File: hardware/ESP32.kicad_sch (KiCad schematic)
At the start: 17 parts, among them J1 USB_C_Receptacle_USB2.0_16P, SW1 SW_Omron_B3FS, SW2 SW_Omron_B3FS, U2 ESP32-C3-WROOM-02, U8 USBLC6-2SC6

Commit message: Found all diodes & transistors footprint & JLCPCB
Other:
- company: (none) -> ECAM Brussels Engineering School
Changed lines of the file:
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@@
 	(generator_version "9.0")
 	(paper "A4")
+	(title_block
+		(rev "0.1")
+		(company "ECAM Brussels Engineering School")
+	)
 	(junction
 		(at 129.54 49.53)

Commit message: Module Lora
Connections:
- net SCL: no longer names the net of R7.2, U2.17 (IO1)
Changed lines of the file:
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@@
+	(wire
+		(pts
+			(xy 184.15 76.2) (xy 198.12 76.2)
+		)
+		(stroke
+			(width 0)
+			(type default)
+		)
+	)
 	(wire
 		(pts
@@
 		)
 		(property "Intersheetrefs" "${INTERSHEET_REFS}"
-			(at 176.0848 68.58 0)
+			(at 175.4197 76.2 0)
 			(effects
 				(font
@@
 		)
 	)
-	(global_label "SCL"
+	(global_label "SPI_CLK"
 		(shape output)
-		(at 177.8 53.34 180)
+		(at 186.69 68.58 180)
 		(fields_autoplaced yes)
 		(effects
@@
 		)
 		(property "Intersheetrefs" "${INTERSHEET_REFS}"
-			(at 171.3072 53.34 0)
+			(at 176.0848 68.58 0)
 			(effects
 				(font

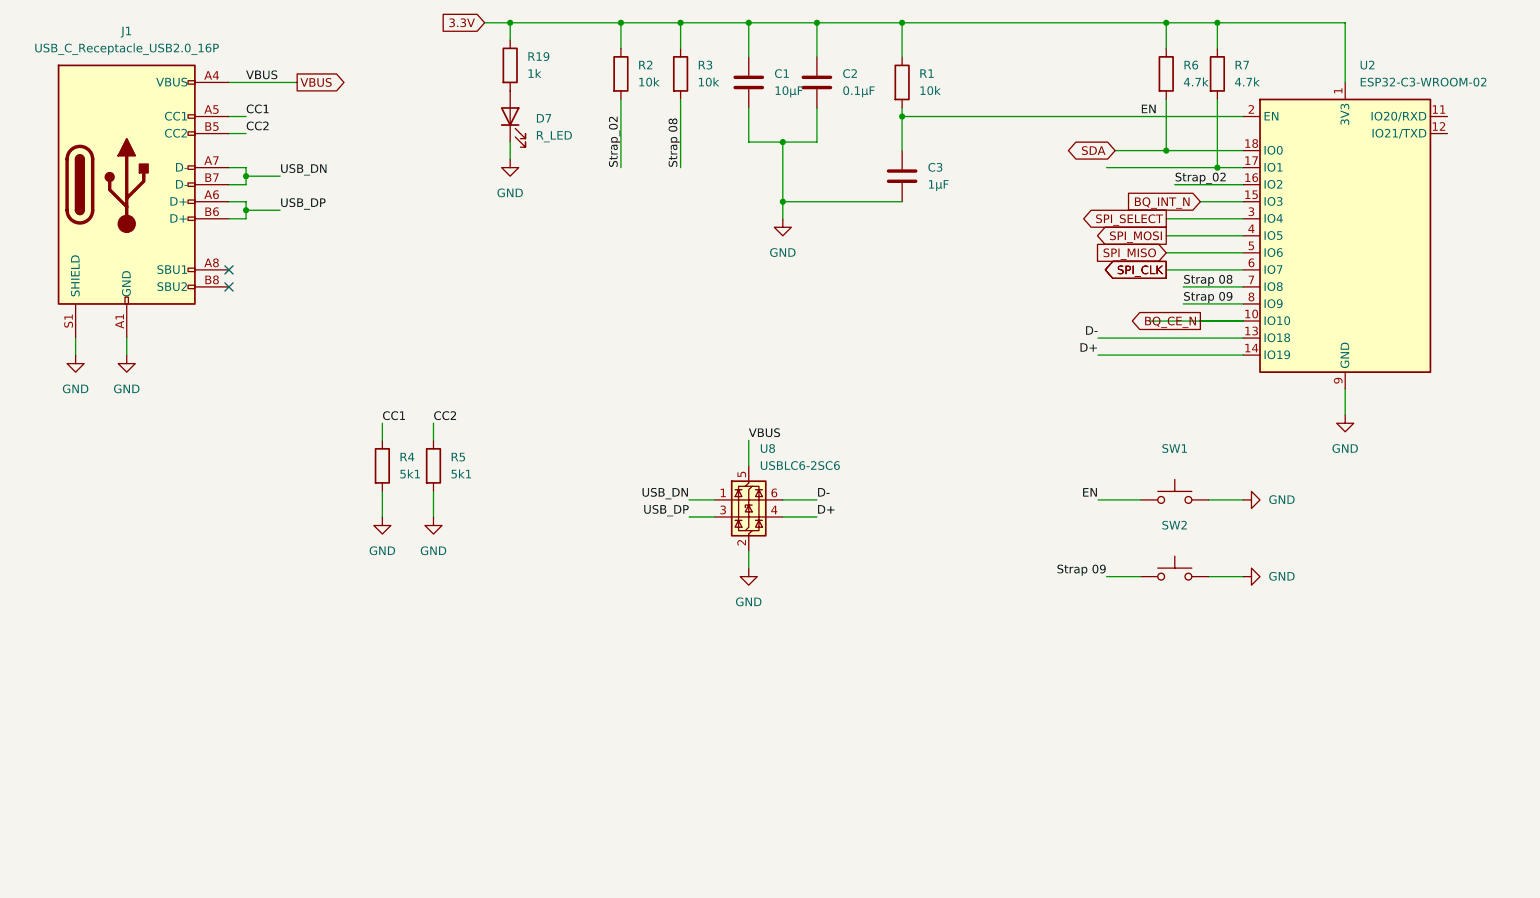
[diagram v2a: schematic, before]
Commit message: Update ESP32 pins
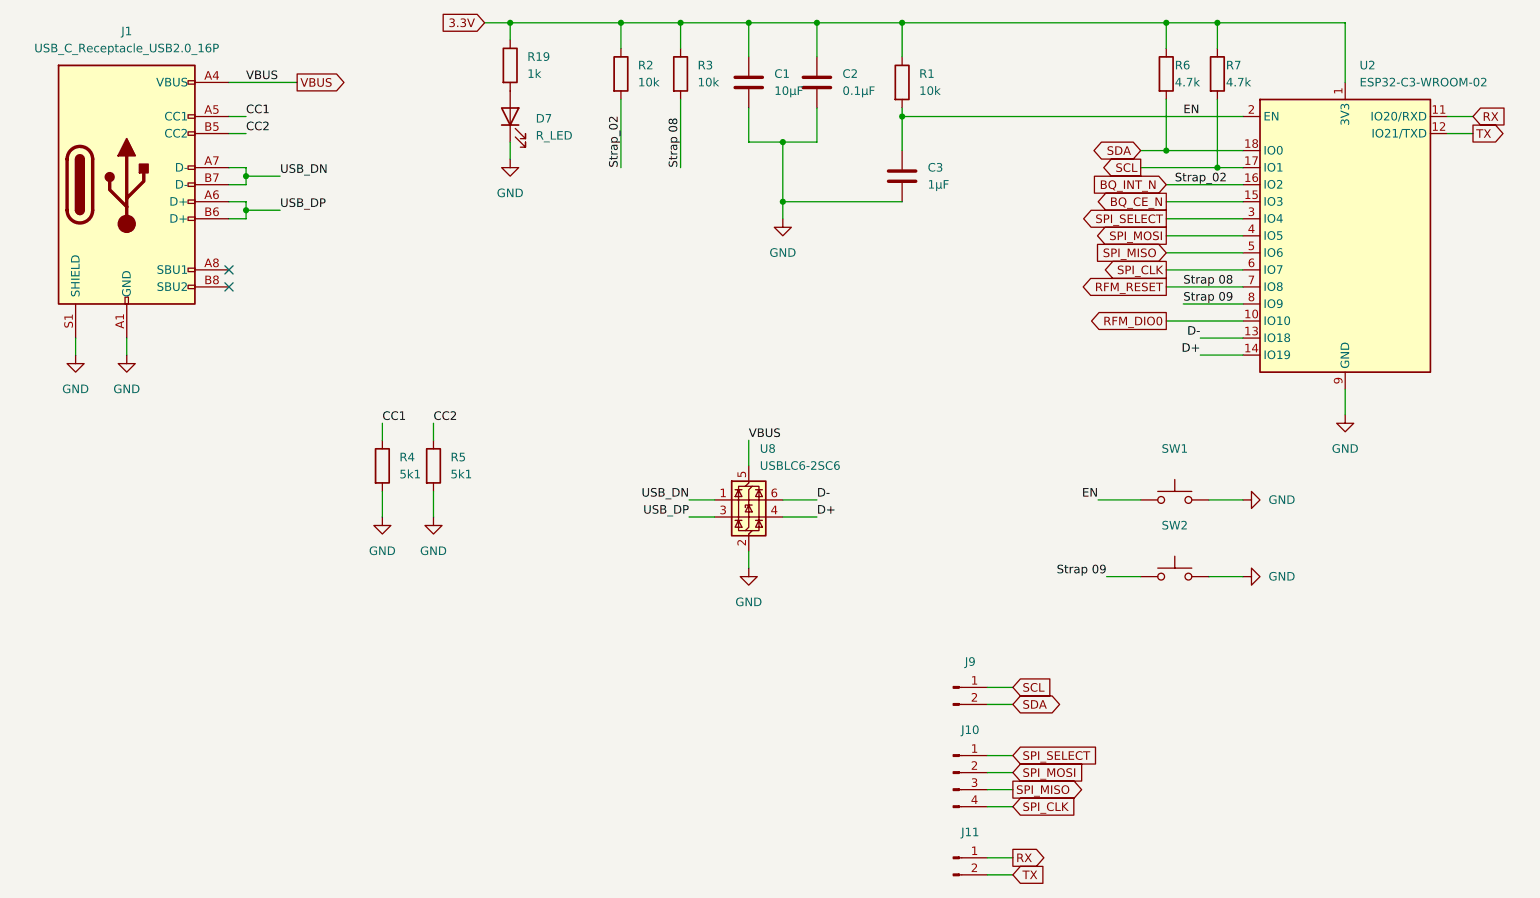
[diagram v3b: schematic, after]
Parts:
- added J10: Conn_01x04_Pin, Connector_PinHeader_2.54mm:PinHeader_1x04_P2.54mm_Vertical, symbol Connector:Conn_01x04_Pin
- added J11, J9: Conn_01x02_Pin, Connector_PinHeader_2.54mm:PinHeader_1x02_P2.54mm_Vertical, symbol Connector:Conn_01x02_Pin
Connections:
- net Strap_02 is gone; now on net BQ_INT_N: R2.2, U2.16 (IO2)
- net BQ_CE_N: now also U2.15 (IO3); no longer U2.10 (IO10)
- net BQ_INT_N: no longer U2.15 (IO3)
- net SDA: now also J9.2 (Pin_2)
- net SPI_CLK: now also J10.4 (Pin_4)
- net SPI_MISO: now also J10.3 (Pin_3)
- net SPI_MOSI: now also J10.2 (Pin_2)
- net SPI_SELECT: now also J10.1 (Pin_1)
- net RX: now reaches U2.11 (IO20/RXD)
- net RX: now also J11.1 (Pin_1)
- net TX: now reaches U2.12 (IO21/TXD)
- net TX: now also J11.2 (Pin_2)
- net SCL: now reaches R7.2, U2.17 (IO1)
- net SCL: now also J9.1 (Pin_1)
- net Strap 08 renamed RFM_RESET
- new net RFM_DIO0: U2.10 (IO10)

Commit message: First draft
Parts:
- renumbered D7 to D1, J9 to J2, J10 to J3, J11 to J4, R4 to R1, R5 to R2, R19 to R3, R2 to R4, R3 to R5, R1 to R6, R6 to R7, R7 to R8, U8 to U1
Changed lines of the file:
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@@
 		(dnp no)
 		(fields_autoplaced yes)
-		(property "Reference" "R4"
+		(property "Reference" "R1"
 			(at 72.39 96.5199 0)
 			(effects
@@
 			(project "GOG"
 				(path "/5b969f6e-a36e-432b-8f00-b2d6a515a877/36e0c9fb-3d9d-4ab1-92fc-4f7433c1320d"
-					(reference "R4")
+					(reference "R1")
 					(unit 1)
 				)
@@
 		(dnp no)
 		(fields_autoplaced yes)
-		(property "Reference" "#PWR02"
+		(property "Reference" "#PWR09"
 			(at 204.47 114.3 0)
 			(effects
@@
 			(project "GOG"
 				(path "/5b969f6e-a36e-432b-8f00-b2d6a515a877/36e0c9fb-3d9d-4ab1-92fc-4f7433c1320d"
-					(reference "#PWR02")
+					(reference "#PWR09")
 					(unit 1)
 				)
@@
 		(on_board yes)
 		(dnp no)
-		(property "Reference" "R6"
+		(property "Reference" "R7"
 			(at 187.96 38.1 0)
 			(effects
@@
 			(project "GOG"
 				(path "/5b969f6e-a36e-432b-8f00-b2d6a515a877/36e0c9fb-3d9d-4ab1-92fc-4f7433c1320d"
-					(reference "R6")
+					(reference "R7")
 					(unit 1)
 				)
@@
 		(dnp no)
 		(fields_autoplaced yes)
-		(property "Reference" "R2"
+		(property "Reference" "R4"
 			(at 107.95 38.0999 0)
 			(effects
@@
 			(project "GOG"
 				(path "/5b969f6e-a36e-432b-8f00-b2d6a515a877/36e0c9fb-3d9d-4ab1-92fc-4f7433c1320d"
-					(reference "R2")
+					(reference "R4")
 					(unit 1)
 				)
@@
 		(on_board yes)
 		(dnp no)
-		(property "Reference" "J10"
+		(property "Reference" "J3"
 			(at 157.48 137.16 0)
 			(effects
@@
 			(project ""
 				(path "/5b969f6e-a36e-432b-8f00-b2d6a515a877/36e0c9fb-3d9d-4ab1-92fc-4f7433c1320d"
-					(reference "J10")
+					(reference "J3")
 					(unit 1)
 				)
@@
 		(on_board yes)
 		(dnp no)
-		(property "Reference" "J11"
+		(property "Reference" "J4"
 			(at 157.48 152.4 0)
 			(effects
@@
 			(project "GOG"
 				(path "/5b969f6e-a36e-432b-8f00-b2d6a515a877/36e0c9fb-3d9d-4ab1-92fc-4f7433c1320d"
-					(reference "J11")
+					(reference "J4")
 					(unit 1)
 				)
@@
 		(dnp no)
 		(fields_autoplaced yes)
-		(property "Reference" "#PWR037"
+		(property "Reference" "#PWR05"
 			(at 88.9 58.42 0)
 			(effects
@@
 			(project "GOG"
 				(path "/5b969f6e-a36e-432b-8f00-b2d6a515a877/36e0c9fb-3d9d-4ab1-92fc-4f7433c1320d"
-					(reference "#PWR037")
+					(reference "#PWR05")
 					(unit 1)
 				)
@@
 		(dnp no)
 		(fields_autoplaced yes)
-		(property "Reference" "R1"
+		(property "Reference" "R6"
 			(at 149.86 39.3699 0)
 			(effects
@@
 			(project "GOG"
 				(path "/5b969f6e-a36e-432b-8f00-b2d6a515a877/36e0c9fb-3d9d-4ab1-92fc-4f7433c1320d"
-					(reference "R1")
+					(reference "R6")
 					(unit 1)
 				)
@@
 		(dnp no)
 		(fields_autoplaced yes)
-		(property "Reference" "#PWR04"
+		(property "Reference" "#PWR08"
 			(at 204.47 102.87 0)
 			(effects
@@
 			(project "GOG"
 				(path "/5b969f6e-a36e-432b-8f00-b2d6a515a877/36e0c9fb-3d9d-4ab1-92fc-4f7433c1320d"
-					(reference "#PWR04")
+					(reference "#PWR08")
 					(unit 1)
 				)
@@
 		(dnp no)
 		(fields_autoplaced yes)
-		(property "Reference" "#PWR03"
+		(property "Reference" "#PWR07"
 			(at 129.54 67.31 0)
 			(effects
@@
 			(project "GOG"
 				(path "/5b969f6e-a36e-432b-8f00-b2d6a515a877/36e0c9fb-3d9d-4ab1-92fc-4f7433c1320d"
-					(reference "#PWR03")
+					(reference "#PWR07")
 					(unit 1)
 				)
@@
 		(dnp no)
 		(fields_autoplaced yes)
-		(property "Reference" "#PWR012"
+		(property "Reference" "#PWR06"
 			(at 124.46 119.38 0)
 			(effects
@@
 			(project "GOG"
 				(path "/5b969f6e-a36e-432b-8f00-b2d6a515a877/36e0c9fb-3d9d-4ab1-92fc-4f7433c1320d"
-					(reference "#PWR012")
+					(reference "#PWR06")
 					(unit 1)
 				)
@@
 		(on_board yes)
 		(dnp no)
-		(property "Reference" "J9"
+		(property "Reference" "J2"
 			(at 157.48 127 0)
 			(effects
@@
 			(project ""
 				(path "/5b969f6e-a36e-432b-8f00-b2d6a515a877/36e0c9fb-3d9d-4ab1-92fc-4f7433c1320d"
-					(reference "J9")
+					(reference "J2")
 					(unit 1)
 				)
@@
 		(dnp no)
 		(fields_autoplaced yes)
-		(property "Reference" "D7"
+		(property "Reference" "D1"
 			(at 92.71 46.0374 90)
 			(effects
@@
 			(project "GOG"
 				(path "/5b969f6e-a36e-432b-8f00-b2d6a515a877/36e0c9fb-3d9d-4ab1-92fc-4f7433c1320d"
-					(reference "D7")
+					(reference "D1")
 					(unit 1)
 				)
@@
 		(dnp no)
 		(fields_autoplaced yes)
-		(property "Reference" "U8"
+		(property "Reference" "U1"
 			(at 126.1111 95.25 0)
 			(effects
@@
 			(project ""
 				(path "/5b969f6e-a36e-432b-8f00-b2d6a515a877/36e0c9fb-3d9d-4ab1-92fc-4f7433c1320d"
-					(reference "U8")
+					(reference "U1")
 					(unit 1)
 				)
@@
 		(dnp no)
 		(fields_autoplaced yes)
-		(property "Reference" "R3"
+		(property "Reference" "R5"
 			(at 116.84 38.0999 0)
 			(effects
@@
 			(project "GOG"
 				(path "/5b969f6e-a36e-432b-8f00-b2d6a515a877/36e0c9fb-3d9d-4ab1-92fc-4f7433c1320d"
-					(reference "R3")
+					(reference "R5")
 					(unit 1)
 				)
@@
 		(dnp no)
 		(fields_autoplaced yes)
-		(property "Reference" "#PWR010"
+		(property "Reference" "#PWR03"
 			(at 69.85 111.76 0)
 			(effects
@@
 			(project "GOG"
 				(path "/5b969f6e-a36e-432b-8f00-b2d6a515a877/36e0c9fb-3d9d-4ab1-92fc-4f7433c1320d"
-					(reference "#PWR010")
+					(reference "#PWR03")
 					(unit 1)
 				)
@@
 		(dnp no)
 		(fields_autoplaced yes)
-		(property "Reference" "R5"
+		(property "Reference" "R2"
 			(at 80.01 96.5199 0)
 			(effects
@@
 			(project "GOG"
 				(path "/5b969f6e-a36e-432b-8f00-b2d6a515a877/36e0c9fb-3d9d-4ab1-92fc-4f7433c1320d"
-					(reference "R5")
+					(reference "R2")
 					(unit 1)
 				)
@@
 		(dnp no)
 		(fields_autoplaced yes)
-		(property "Reference" "#PWR01"
+		(property "Reference" "#PWR010"
 			(at 213.36 96.52 0)
 			(effects
@@
 			(project "GOG"
 				(path "/5b969f6e-a36e-432b-8f00-b2d6a515a877/36e0c9fb-3d9d-4ab1-92fc-4f7433c1320d"
-					(reference "#PWR01")
+					(reference "#PWR010")
 					(unit 1)
 				)
@@
 		(dnp no)
 		(fields_autoplaced yes)
-		(property "Reference" "#PWR016"
+		(property "Reference" "#PWR02"
 			(at 31.75 87.63 0)
 			(effects
@@
 			(project "GOG"
 				(path "/5b969f6e-a36e-432b-8f00-b2d6a515a877/36e0c9fb-3d9d-4ab1-92fc-4f7433c1320d"
-					(reference "#PWR016")
+					(reference "#PWR02")
 					(unit 1)
 				)
@@
 		(dnp no)
 		(fields_autoplaced yes)
-		(property "Reference" "#PWR015"
+		(property "Reference" "#PWR01"
 			(at 24.13 87.63 0)
 			(effects
@@
 			(project "GOG"
 				(path "/5b969f6e-a36e-432b-8f00-b2d6a515a877/36e0c9fb-3d9d-4ab1-92fc-4f7433c1320d"
-					(reference "#PWR015")
+					(reference "#PWR01")
 					(unit 1)
 				)
@@
 		(on_board yes)
 		(dnp no)
-		(property "Reference" "R7"
+		(property "Reference" "R8"
 			(at 195.58 38.1 0)
 			(effects
@@
 			(project "GOG"
 				(path "/5b969f6e-a36e-432b-8f00-b2d6a515a877/36e0c9fb-3d9d-4ab1-92fc-4f7433c1320d"
-					(reference "R7")
+					(reference "R8")
 					(unit 1)
 				)
@@
 		(dnp no)
 		(fields_autoplaced yes)
-		(property "Reference" "#PWR011"
+		(property "Reference" "#PWR04"
 			(at 77.47 111.76 0)
 			(effects
@@
 			(project "GOG"
 				(path "/5b969f6e-a36e-432b-8f00-b2d6a515a877/36e0c9fb-3d9d-4ab1-92fc-4f7433c1320d"
-					(reference "#PWR011")
+					(reference "#PWR04")
 					(unit 1)
 				)
@@
 		(dnp no)
 		(fields_autoplaced yes)
-		(property "Reference" "R19"
+		(property "Reference" "R3"
 			(at 91.44 36.8299 0)
 			(effects
@@
 			(project "GOG"
 				(path "/5b969f6e-a36e-432b-8f00-b2d6a515a877/36e0c9fb-3d9d-4ab1-92fc-4f7433c1320d"
-					(reference "R19")
-					(unit 1)
-				)
+					(reference "R3")
+					(unit 1)
+				)
